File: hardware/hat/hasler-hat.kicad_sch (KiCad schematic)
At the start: 112 parts, among them J1 Amp4 top header, J2 Hasler J2, J3 USB-C PD in, J4 Debug / expansion, J5 Qwiic, J6 To Amp4 DC in, Q1 AO4407A, Q2 2N7002, U1 MCP23017, U10 SRV05-4, U11 SRV05-4, U12 SRV05-4, U2 ADS1115, U3 CH224A, U4 LM393, U5 AZ431AN, U6 XC6206P332MR, U7 SRV05-4, U8 SRV05-4, U9 SRV05-4

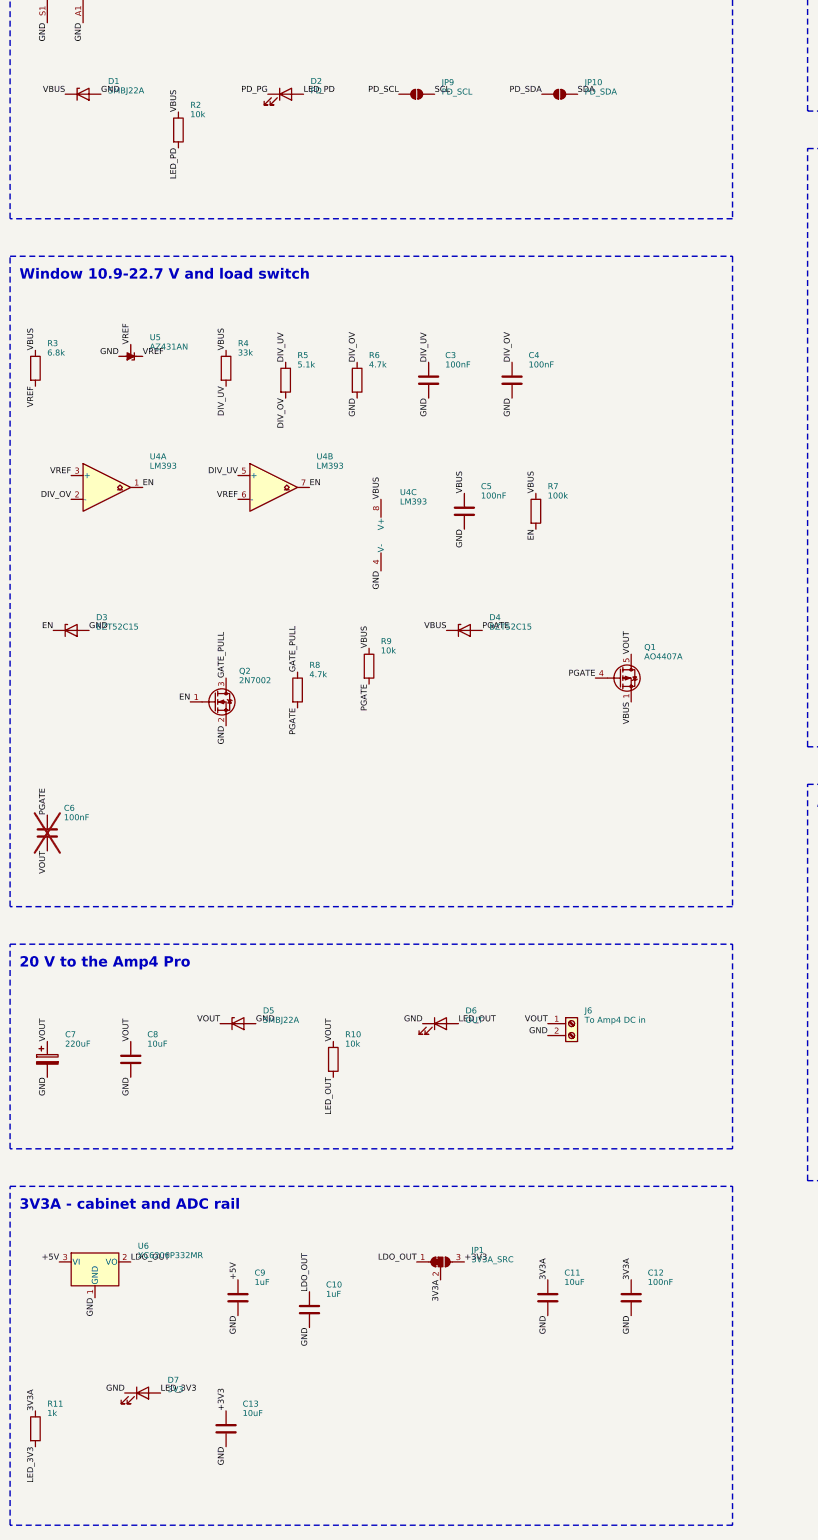
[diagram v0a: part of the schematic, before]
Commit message: HAT: review fixes - soft start fitted, 1 nF divider filters, UV hysteresis on its own divider, X7R VHV cap, AZ431 ATRG1; 85 mm board placement
Co-Authored-By: Claude Opus 5.5 <noreply@anthropic.com>
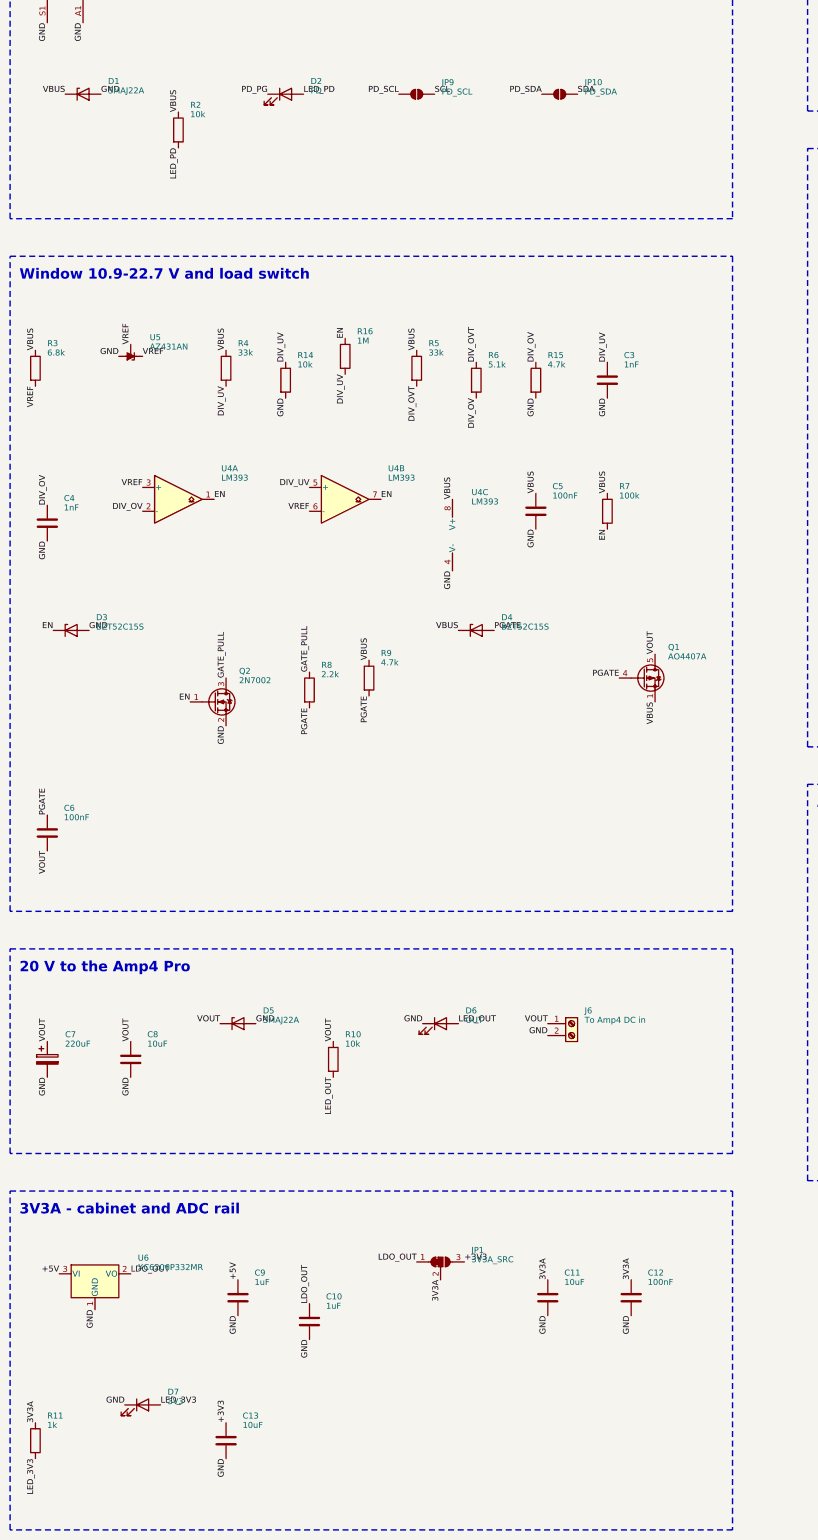
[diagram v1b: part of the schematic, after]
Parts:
- added R14: 10k, Resistor_SMD:R_0603_1608Metric, symbol Device:R
- added R15: 4.7k, Resistor_SMD:R_0603_1608Metric, symbol Device:R
- added R16: 1M, Resistor_SMD:R_0603_1608Metric, symbol Device:R
- C1: footprint Capacitor_SMD:C_0603_1608Metric -> Capacitor_SMD:C_0805_2012Metric; LCSC C15849 -> C28323
- C12, C14, C15, C20, C21, C22, C23, C24, C25, C26, C27, C28, C29, C30, C31, C32, C33, C34, C35, C36, C37: footprint Capacitor_SMD:C_0603_1608Metric -> Capacitor_SMD:C_0402_1005Metric; LCSC C14663 -> C1525
- C3, C4: value 100nF -> 1nF; LCSC C14663 -> C1588; MPN 100nF -> 1nF
- C6: now fitted
- D1, D5: value SMBJ22A -> SMAJ22A; footprint Diode_SMD:D_SMB -> Diode_SMD:D_SMA; LCSC C113993 -> C283896; MPN SMBJ22A -> SMAJ22A
- D3, D4: value BZT52C15 -> BZT52C15S; footprint Diode_SMD:D_SOD-123 -> Diode_SMD:D_SOD-323; LCSC C173427 -> C17283; MPN BZT52C15 -> BZT52C15S
- J6: footprint TerminalBlock_Phoenix:TerminalBlock_Phoenix_MKDS-1,5-2-5.08_1x02_P5.08mm_Horizontal -> TerminalBlock_Phoenix:TerminalBlock_Phoenix_PT-1,5-2-3.5-H_1x02_P3.50mm_Horizontal; LCSC C474952 -> C474892; MPN KF128-5.08-2P -> KF350-3.5-2P
- R5: value 5.1k -> 33k; LCSC C23186 -> C4216; MPN 5.1k -> 33k
- R6: value 4.7k -> 5.1k; LCSC C23162 -> C23186; MPN 4.7k -> 5.1k
- R8: value 4.7k -> 2.2k; LCSC C23162 -> C4190; MPN 4.7k -> 2.2k
- R9: value 10k -> 4.7k; LCSC C25804 -> C23162; MPN 10k -> 4.7k
- TP1, TP10, TP11, TP12, TP13, TP14, TP2, TP3, TP4, TP5, TP6, TP7, TP8, TP9: footprint TestPoint:TestPoint_Pad_D1.5mm -> TestPoint:TestPoint_Pad_D1.0mm
- U1: footprint Package_SO:SOIC-28W_7.5x17.9mm_P1.27mm -> Package_SO:SSOP-28_5.3x10.2mm_P0.65mm; LCSC C47023 -> C506653; MPN MCP23017-E/SO -> MCP23017-E/SS
- U5: LCSC C84138 -> C92573; MPN AZ431AN-ATRE1 -> AZ431AN-ATRG1
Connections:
- net DIV_OV: now also R6.2, R15.1; no longer R5.2, R6.1
- net DIV_UV: now also R14.1, R16.2; no longer R5.1
- net EN: now also R16.1
- net GND: now also R14.2, R15.2; no longer R6.2
- net VBUS: now also R5.1
- new net DIV_OVT: R5.2, R6.1
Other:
- moved on the sheet: C10, C13, C3, C4, C5, D4, D7, Q1, R11, R5, R6, R7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

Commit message: HAT: complete routing - GND fan-out before routing, pre-routed power paths, VOUT trunk, notch for the Amp4 cap, gap closer; pull-ups to the cabinet side
Co-Authored-By: Claude Opus 5.5 <noreply@anthropic.com>
Claude-Session: https://claude.ai/code/session_014wovV18Ypx4LXt9k8BSCRk
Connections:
- net J_A0: now also RN5.1 (R1.1); no longer RN2.4 (R4.1)
- net J_A1: now also RN5.2 (R2.1); no longer RN3.1 (R1.1)
- net J_A2: now also RN5.3 (R3.1); no longer RN5.1 (R1.1)
- net J_A3: now also RN5.4 (R4.1); no longer RN5.2 (R2.1)
- net J_K1: now also RN6.8 (R1.2)
- net J_K2: now also RN6.7 (R2.2)
- net J_K3: now also RN6.6 (R3.2)
- net J_K4: now also RN6.5 (R4.2)
- net J_K5: now also RN7.8 (R1.2)
- net J_K6: now also RN7.7 (R2.2)
- net J_PU: now also RN7.6 (R3.2)
- net J_TSW: now also RN2.4 (R4.1), RN7.5 (R4.2); no longer RN3.2 (R2.1)
- net J_X1: now also RN3.1 (R1.1), RN8.8 (R1.2); no longer RN3.3 (R3.1)
- net J_X2: now also RN3.2 (R2.1), RN8.7 (R2.2); no longer RN3.4 (R4.1)
- net J_X3: now also RN3.3 (R3.1), RN8.6 (R3.2); no longer RN4.1 (R1.1)
- net J_X4: now also RN3.4 (R4.1), RN8.5 (R4.2); no longer RN4.2 (R2.1)
- net J_X5: now also RN4.1 (R1.1), RN9.8 (R1.2); no longer RN4.3 (R3.1)
- net J_X6: now also RN4.2 (R2.1), RN9.7 (R2.2); no longer RN4.4 (R4.1)
- net M_A0: now also C34.1, RN5.8 (R1.2); no longer C27.1, RN2.5 (R4.2)
- net M_A1: now also C35.1, RN5.7 (R2.2); no longer C28.1, RN3.8 (R1.2)
- net M_A2: now also RN5.6 (R3.2); no longer RN5.8 (R1.2)
- net M_A3: now also RN5.5 (R4.2); no longer RN5.7 (R2.2)
- net M_K1: no longer RN6.8 (R1.2)
- net M_K2: no longer RN6.7 (R2.2)
- net M_K3: no longer RN6.6 (R3.2)
- net M_K4: no longer RN6.5 (R4.2)
- net M_K5: no longer RN7.8 (R1.2)
- net M_K6: no longer RN7.7 (R2.2)
- net M_PU: no longer RN7.6 (R3.2)
- net M_TSW: now also C27.1, RN2.5 (R4.2); no longer C29.1, RN3.7 (R2.2), RN7.5 (R4.2)
- net M_X1: now also C28.1, RN3.8 (R1.2); no longer C30.1, RN3.6 (R3.2), RN8.8 (R1.2)
- net M_X2: now also C29.1, RN3.7 (R2.2); no longer C31.1, RN3.5 (R4.2), RN8.7 (R2.2)
- net M_X3: now also C30.1, RN3.6 (R3.2); no longer C32.1, RN4.8 (R1.2), RN8.6 (R3.2)
- net M_X4: now also C31.1, RN3.5 (R4.2); no longer C33.1, RN4.7 (R2.2), RN8.5 (R4.2)
- net M_X5: now also C32.1, RN4.8 (R1.2); no longer C34.1, RN4.6 (R3.2), RN9.8 (R1.2)
- net M_X6: now also C33.1, RN4.7 (R2.2); no longer C35.1, RN4.5 (R4.2), RN9.7 (R2.2)
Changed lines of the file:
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@@
 	)
 	(no_connect
-		(at 408.94 254)
+		(at 386.08 254)
 	)
 	(no_connect
-		(at 408.94 264.16)
+		(at 386.08 264.16)
 	)
 	(no_connect
-		(at 411.48 254)
+		(at 388.62 254)
 	)
 	(no_connect
-		(at 411.48 264.16)
+		(at 388.62 264.16)
 	)
 	(no_connect
@@
 		)
 	)
-	(label "M_A0"
+	(label "M_TSW"
 		(at 345.44 254 90)
 		(fields_autoplaced yes)
@@
 		)
 	)
-	(label "J_A0"
+	(label "J_TSW"
 		(at 345.44 264.16 270)
 		(fields_autoplaced yes)
@@
 		)
 	)
-	(label "M_A1"
+	(label "M_X1"
 		(at 358.14 254 90)
 		(fields_autoplaced yes)
@@
 		)
 	)
-	(label "J_A1"
+	(label "J_X1"
 		(at 358.14 264.16 270)
 		(fields_autoplaced yes)
@@
 		)
 	)
-	(label "M_TSW"
+	(label "M_X2"
 		(at 360.68 254 90)
 		(fields_autoplaced yes)
@@
 		)
 	)
-	(label "J_TSW"
+	(label "J_X2"
 		(at 360.68 264.16 270)
 		(fields_autoplaced yes)
@@
 		)
 	)
-	(label "M_X1"
+	(label "M_X3"
 		(at 363.22 254 90)
 		(fields_autoplaced yes)
@@
 		)
 	)
-	(label "J_X1"
+	(label "J_X3"
 		(at 363.22 264.16 270)
 		(fields_autoplaced yes)
@@
 		)
 	)
-	(label "M_X2"
+	(label "M_X4"
 		(at 365.76 254 90)
 		(fields_autoplaced yes)
@@
 		)
 	)
-	(label "J_X2"
+	(label "J_X4"
 		(at 365.76 264.16 270)
 		(fields_autoplaced yes)
@@
 		)
 	)
-	(label "M_X3"
+	(label "M_X5"
 		(at 381 254 90)
 		(fields_autoplaced yes)
@@
 		)
 	)
-	(label "J_X3"
+	(label "J_X5"
 		(at 381 264.16 270)
 		(fields_autoplaced yes)
@@
 		)
 	)
-	(label "M_X4"
+	(label "M_X6"
 		(at 383.54 254 90)
 		(fields_autoplaced yes)
@@
 		)
 	)
-	(label "J_X4"
+	(label "J_X6"
 		(at 383.54 264.16 270)
 		(fields_autoplaced yes)
@@
 		)
 	)
-	(label "M_X5"
-		(at 386.08 254 90)
+	(label "M_A0"
+		(at 403.86 254 90)
 		(fields_autoplaced yes)
 		(effects
@@
 		)
 	)
-	(label "J_X5"
-		(at 386.08 264.16 270)
+	(label "J_A0"
+		(at 403.86 264.16 270)
 		(fields_autoplaced yes)
 		(effects
@@
 		)
 	)
-	(label "M_X6"
-		(at 388.62 254 90)
+	(label "M_A1"
+		(at 406.4 254 90)
 		(fields_autoplaced yes)
 		(effects
@@
 		)
 	)
-	(label "J_X6"
-		(at 388.62 264.16 270)
+	(label "J_A1"
+		(at 406.4 264.16 270)
 		(fields_autoplaced yes)
 		(effects
@@
 	)
 	(label "M_A2"
-		(at 403.86 254 90)
+		(at 408.94 254 90)
 		(fields_autoplaced yes)
 		(effects
@@
 	)
 	(label "J_A2"
-		(at 403.86 264.16 270)
+		(at 408.94 264.16 270)
 		(fields_autoplaced yes)
 		(effects
@@
 	)
 	(label "M_A3"
-		(at 406.4 254 90)
+		(at 411.48 254 90)
 		(fields_autoplaced yes)
 		(effects
@@
 	)
 	(label "J_A3"
-		(at 406.4 264.16 270)
+		(at 411.48 264.16 270)
 		(fields_autoplaced yes)
 		(effects
@@
 		)
 	)
-	(label "M_K1"
+	(label "J_K1"
 		(at 426.72 254 90)
 		(fields_autoplaced yes)
@@
 		)
 	)
-	(label "M_K2"
+	(label "J_K2"
 		(at 429.26 254 90)
 		(fields_autoplaced yes)
@@
 		)
 	)
-	(label "M_K3"
+	(label "J_K3"
 		(at 431.8 254 90)
 		(fields_autoplaced yes)
@@
 		)
 	)
-	(label "M_K4"
+	(label "J_K4"
 		(at 434.34 254 90)
 		(fields_autoplaced yes)
@@
 		)
 	)
-	(label "M_K5"
+	(label "J_K5"
 		(at 449.58 254 90)
 		(fields_autoplaced yes)
@@
 		)
 	)
-	(label "M_K6"
+	(label "J_K6"
 		(at 452.12 254 90)
 		(fields_autoplaced yes)
@@
 		)
 	)
-	(label "M_PU"
+	(label "J_PU"
 		(at 454.66 254 90)
 		(fields_autoplaced yes)
@@
 		)
 	)
-	(label "M_TSW"
+	(label "J_TSW"
 		(at 457.2 254 90)
 		(fields_autoplaced yes)
@@
 		)
 	)
-	(label "M_X1"
+	(label "J_X1"
 		(at 337.82 284.48 90)
 		(fields_autoplaced yes)
@@
 		)
 	)
-	(label "M_X2"
+	(label "J_X2"
 		(at 340.36 284.48 90)
 		(fields_autoplaced yes)
@@
 		)
 	)
-	(label "M_X3"
+	(label "J_X3"
 		(at 342.9 284.48 90)
 		(fields_autoplaced yes)
@@
 		)
 	)
-	(label "M_X4"
+	(label "J_X4"
 		(at 345.44 284.48 90)
 		(fields_autoplaced yes)
@@
 		)
 	)
-	(label "M_X5"
+	(label "J_X5"
 		(at 360.68 284.48 90)
 		(fields_autoplaced yes)
@@
 		)
 	)
-	(label "M_X6"
+	(label "J_X6"
 		(at 363.22 284.48 90)
 		(fields_autoplaced yes)
@@
 		)
 	)
-	(label "M_A0"
+	(label "M_TSW"
 		(at 373.38 313.69 90)
 		(fields_autoplaced yes)
@@
 		)
 	)
-	(label "M_A1"
+	(label "M_X1"
 		(at 391.16 313.69 90)
 		(fields_autoplaced yes)
@@
 		)
 	)
-	(label "M_TSW"
+	(label "M_X2"
 		(at 408.94 313.69 90)
 		(fields_autoplaced yes)
@@
 		)
 	)
-	(label "M_X1"
+	(label "M_X3"
 		(at 424.18 313.69 90)
 		(fields_autoplaced yes)
@@
 		)
 	)
-	(label "M_X2"
+	(label "M_X4"
 		(at 441.96 313.69 90)
 		(fields_autoplaced yes)
@@
 		)
 	)
-	(label "M_X3"
+	(label "M_X5"
 		(at 337.82 339.09 90)
 		(fields_autoplaced yes)
@@
 		)
 	)
-	(label "M_X4"
+	(label "M_X6"
 		(at 355.6 339.09 90)
 		(fields_autoplaced yes)
@@
 		)
 	)
-	(label "M_X5"
+	(label "M_A0"
 		(at 373.38 339.09 90)
 		(fields_autoplaced yes)
@@
 		)
 	)
-	(label "M_X6"
+	(label "M_A1"
 		(at 391.16 339.09 90)
 		(fields_autoplaced yes)

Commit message: HAT: review fixes - notch over the standing cap, soft start, VBUS strap, keepouts, thermals, silkscreen
From the five-reviewer pass:
- notch moved to x 11.5-22.5 (HAT coords): the Amp4's 8 mm cap stands over
  leads at x 15.13/18.93; the old notch came from the lying-down model
- turn-on: C6 470 nF (Miller, ~1.4-3.5 A inrush instead of 7-16 A),
  C17 10 uF gate-source (a fast VBUS edge can't turn the FET on), C18 1 uF on
  EN (waits out the PD transition)
- R13 (ADS RDY pull-up) to the Pi's 3V3; 100 nF at every SRV05-4 VCC
- J3's VBUS pad pairs joined by a bottom-layer strap under the pad row;
  CH224A VHV-VBUS, CC1 and D+ laid through vias before routing
- no tracks/vias within 3 mm of the mounting holes; thermal spokes on THT GND
- silkscreen >= 1.0 mm text, >= 0.15 mm lines; J2 pin 1 marked inboard
- build.sh stops on DRC errors; gap-closer and width passes reworked
- ORDERING.md: J1 hand-soldered, review options, bring-up checks; DESIGN.md

DRC 0 / 0 unconnected / parity clean, ERC 0.

Co-Authored-By: Claude Opus 5.5 <noreply@anthropic.com>
Claude-Session: https://claude.ai/code/session_014wovV18Ypx4LXt9k8BSCRk
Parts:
- added C17: 10uF, Capacitor_SMD:C_0805_2012Metric, symbol Device:C
- added C18: 1uF, Capacitor_SMD:C_0402_1005Metric, symbol Device:C
- added C38, C39, C40, C41, C42, C43: 100nF, Capacitor_SMD:C_0402_1005Metric, symbol Device:C
- C6: value 100nF -> 470nF; footprint Capacitor_SMD:C_0603_1608Metric -> Capacitor_SMD:C_0805_2012Metric; LCSC C14663 -> C13967; MPN 100nF -> 470nF
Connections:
- net +3V3: now also R13.1
- net 3V3A: now also C38.1, C39.1, C40.1, C41.1, C42.1, C43.1; no longer R13.1
- net EN: now also C18.1
- net GND: now also C18.2, C38.2, C39.2, C40.2, C41.2, C42.2, C43.2
- net PGATE: now also C17.1
- net VBUS: now also C17.2
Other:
- moved on the sheet: C11, C12, C20, C21, C22, C23, C24, C25, C26, C27, C28, C29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

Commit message: HAT: TPS259474A eFuse replaces the discrete window + P-FET; second VBUS path; routing fixes
Second review round: the discrete soft start (C6 470 nF + C17 10 uF) made the
inrush scale with the Amp4's unknown input capacitance and slowed OV turn-off to
~50 ms. U4 is now a TI TPS259474A (C3662807): UVLO 11.2 V, OVLO 23.0 V in 1.2 us,
dV/dt 0.9 V/ms (0.9 A into 1000 uF), 3.3 A circuit breaker with 18 ms blanking,
true reverse-current blocking, PG to TP12. Footprint hasler:TI_RPW0010A built
from TI's land pattern (no KiCad library part).

Also: a second B.Cu path from J3's VBUS strap to D1; LEDs turned to face their
resistors; CH224A I2C stubs and the MCP-ADS SDA link laid before routing; the
gap-closer gains a two-via fallback and stops when it stalls. DRC 0/0, ERC 0.

Co-Authored-By: Claude Opus 5.5 <noreply@anthropic.com>
Claude-Session: https://claude.ai/code/session_014wovV18Ypx4LXt9k8BSCRk
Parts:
- removed C17: 10uF, Capacitor_SMD:C_0805_2012Metric, symbol Device:C
- removed C18: 1uF, Capacitor_SMD:C_0402_1005Metric, symbol Device:C
- removed C6: 470nF, Capacitor_SMD:C_0805_2012Metric, symbol Device:C
- removed D3, D4: BZT52C15S, Diode_SMD:D_SOD-323, symbol Device:D_Zener
- removed Q1: AO4407A, Package_SO:SOIC-8_3.9x4.9mm_P1.27mm, symbol Transistor_FET:IRF7404
- removed Q2: 2N7002, Package_TO_SOT_SMD:SOT-23, symbol Transistor_FET:2N7002
- removed R16: 1M, Resistor_SMD:R_0603_1608Metric, symbol Device:R
- removed unit 2 of U4
- removed unit 3 of U4
- removed U5: AZ431AN, Package_TO_SOT_SMD:SOT-23, symbol hasler:AZ431_SOT23
- C3: value 1nF -> 2.2nF; LCSC C1588 -> C1604; MPN 1nF -> 2.2nF
- C4: value 1nF -> 22nF; footprint Capacitor_SMD:C_0603_1608Metric -> Capacitor_SMD:C_0402_1005Metric; LCSC C1588 -> C1532; MPN 1nF -> 22nF
- C5: value 100nF -> 1uF; LCSC C14663 -> C15849; MPN 100nF -> 1uF
- R14: value 10k -> 1k; footprint Resistor_SMD:R_0603_1608Metric -> Resistor_SMD:R_0402_1005Metric; LCSC C25804 -> C11702; MPN 10k -> 1k
- R15: value 4.7k -> 10k; LCSC C23162 -> C25804; MPN 4.7k -> 10k
- R3: value 6.8k -> 1M; LCSC C23212 -> C22935; MPN 6.8k -> 1M
- R4: value 33k -> 120k; LCSC C4216 -> C25808; MPN 33k -> 120k
- R5: value 33k -> 2M; LCSC C4216 -> C22976; MPN 33k -> 2M
- R6: value 5.1k -> 100k; LCSC C23186 -> C25803; MPN 5.1k -> 100k
- R7: value 100k -> 10k; LCSC C25803 -> C25804; MPN 100k -> 10k
- R8: value 2.2k -> 1M; LCSC C4190 -> C22935; MPN 2.2k -> 1M
- R9: value 4.7k -> 120k; LCSC C23162 -> C25808; MPN 4.7k -> 120k
- TP11: value PG -> PD; MPN PG -> PD
- TP12: value EN -> PG; MPN EN -> PG
- U4: value LM393 -> TPS259474ARPWR; footprint Package_SO:SOIC-8_3.9x4.9mm_P1.27mm -> hasler:TI_RPW0010A_VQFN-HR-10_2x2mm_P0.45mm; symbol Comparator:LM393 -> hasler:TPS259474; LCSC C7955 -> C3662807; MPN LM393DR2G -> TPS259474ARPWR
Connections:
- net GATE_PULL is gone; now on net VOUT: R8.1
- net +3V3: now also R15.1
- net GND: now also R4.2, R7.2, R9.2, U4.8 (GND); no longer R15.2
- net VBUS: now also U4.5 (IN); no longer R4.1, R7.1, R9.1
- net VOUT: now also U4.6 (OUT)
- removed net DIV_OV: C4.1, R15.1, R6.2, U4.2 (-)
- net DIV_OVT renamed EF_OV
- net EF_OV: now also U4.2 (OVLO)
- removed net DIV_UV: C3.1, R14.1, R4.2
- removed net EN: R7.2, TP12.1, U4.1
- net PGATE renamed EF_PGTH
- net EF_PGTH: now also R9.1, U4.4 (PGTH); no longer R9.2
- net VREF renamed EF_EN
- net EF_EN: now also R4.1, U4.1 (EN/UVLO); no longer U4.3 (+)
- new net EF_DVDT: C3.1, U4.7 (DVDT)
- new net EF_ILM: R14.1, U4.9 (ILM)
- new net EF_OVB: R6.2, R7.1
- new net EF_PG: R15.2, TP12.1, U4.3 (PG)
- new net EF_TMR: C4.1, U4.10 (ITIMER)
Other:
- note added: "U4 TPS259474 in TI's RPW (VQFN-HR 2x2): footprint hasler:TI_RPW0010A_VQFN-HR-10_2x2mm_P0.45mm."
- note added: "eFuse TPS259474: on 11.2-23 V, 0.9 V/ms, 3.3 A"
- note removed: "AZ431 SOT23 pinout is 1 REF / 2 K / 3 A - NOT the TL431DBZ's. Symbol hasler:AZ431_SOT23."
- note removed: "Window 10.9-22.7 V and load switch"
- moved on the sheet: C10, C11, C12, C13, C3, C4, C5, C7, C8, C9, D5, D6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

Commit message: HAT: eFuse review fixes - thresholds for tolerance, C7 not fitted, IN/OUT ceramics and heat copper
Third review round (eFuse circuit + layout/fab):
- UVLO 10.3 V (R4 120k + R16 12k): a 12 V -5 % contract starts in the worst
  case; OVLO 22.6 V (R7 12k): 21.7-23.7 V worst case, under the amp's 24 V
- C7 (220 uF) not fitted: the eFuse has no power limit at start-up, so VOUT
  capacitance sets its heating; the Amp4 has its own input cap
- C17 1 uF on the OUT run, C5 moved onto the IN run, small VBUS/VOUT pours on
  F/B.Cu with vias round U4 (no exposed pad: the strips are the heat path)
- footprint to TI's exact land pattern (gen/make_fp.py), 82 % paste on IN/OUT
- second vias on the VBUS strap and D1 path; C41/C42 short to their ESD arrays
- R15 100k; docs: start-up check, barrel-jack limit, counts; hardware.md note

DRC 0/0, ERC 0. BOM 35 lines / 89 placements.

Co-Authored-By: Claude Opus 5.5 <noreply@anthropic.com>
Claude-Session: https://claude.ai/code/session_014wovV18Ypx4LXt9k8BSCRk
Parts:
- added C17: 1uF, Capacitor_SMD:C_0603_1608Metric, symbol Device:C
- added R16: 12k, Resistor_SMD:R_0603_1608Metric, symbol Device:R
- C7: now not fitted
- R15: value 10k -> 100k; LCSC C25804 -> C25803; MPN 10k -> 100k
- R7: value 10k -> 12k; LCSC C25804 -> C22790; MPN 10k -> 12k
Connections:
- net GND: now also C17.2, R16.2; no longer R4.2
- net VOUT: now also C17.1
- new net EF_ENB: R16.1, R4.2
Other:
- moved on the sheet: C3, C4, R14, R15, R5, R6, R7, R8, R9
